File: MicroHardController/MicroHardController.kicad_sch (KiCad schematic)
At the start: 4 parts, among them J1 Conn_01x07_Pin, SW1 SW_Push_LED, U1 THB001P

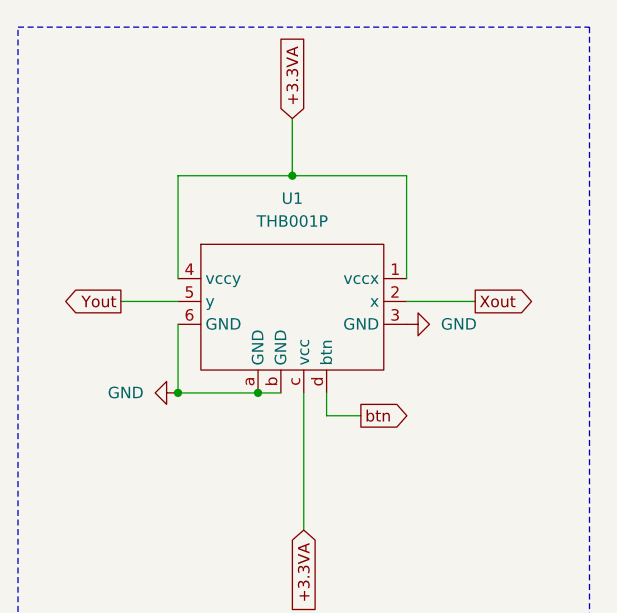
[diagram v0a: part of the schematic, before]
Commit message: feat: microhard controller schematic
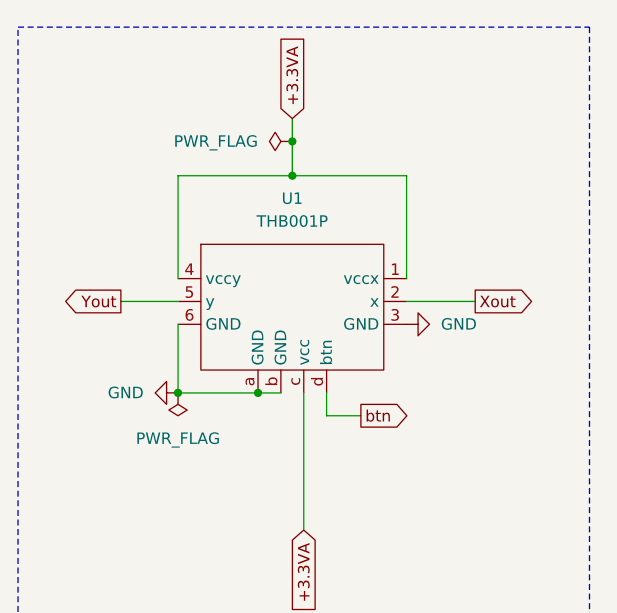
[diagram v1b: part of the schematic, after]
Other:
- company: (none) -> MicroHard
- title: (none) -> MicroHard FlightSimulator Controller

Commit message: feat: controller pcb layout
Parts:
- removed RV1: R_Potentiometer, symbol Device:R_Potentiometer
- added VR1: PS100-1B1BR10K, MicroHard:TRIM_PS100-1B1BR10K, symbol PS100-1B1BR10K:PS100-1B1BR10K
- J1: footprint (none) -> Connector_PinHeader_2.54mm:PinHeader_1x07_P2.54mm_Vertical
- SW1: footprint (none) -> Connector_PinHeader_2.54mm:PinHeader_1x04_P2.54mm_Vertical
- U1: footprint (none) -> MicroHard:CNK_THB001P
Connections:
- net +3.3VA: now also U1.VR1_1 (vccx), U1.VR2_1 (vccy), VR1.1; no longer U1.1 (vccx), U1.4 (vccy), U1.c (vcc)
- net GND: now also U1.VR1_3 (GND), U1.VR2_3 (GND), VR1.3; no longer U1.3 (GND), U1.6 (GND), U1.a (GND), U1.b (GND)
- net Xout: now also U1.VR1_2 (x); no longer U1.2 (x)
- net Yout: now also U1.VR2_2 (y); no longer U1.5 (y)
- net Zout: now also VR1.2
- net btn: no longer names the net of J1.7 (Pin_7)
- net btn: no longer U1.d (btn)
- no-connect marks 0 -> 5

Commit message: fix: controller fix
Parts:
- added R1, R2: 100K, symbol Device:R
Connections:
- net +3.3VA: now also U1.A (a)
- net GND: now also R1.2, R2.2
- net Button2: now reaches J1.7 (Pin_7)
- net Button2: now also U1.D (d), R1.1
- net Fbtn renamed Button1
- net Button1: now also R2.1
- no-connect marks 5 -> 2
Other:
- moved on the sheet: SW1

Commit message: feat: controller fixed
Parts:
- R1, R2: footprint (none) -> Resistor_SMD:R_1206_3216Metric_Pad1.30x1.75mm_HandSolder
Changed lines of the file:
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@@
 			)
 		)
-		(property "Footprint" ""
+		(property "Footprint" "Resistor_SMD:R_1206_3216Metric_Pad1.30x1.75mm_HandSolder"
 			(at 169.672 96.52 90)
 			(effects
@@
 			)
 		)
-		(property "Footprint" ""
+		(property "Footprint" "Resistor_SMD:R_1206_3216Metric_Pad1.30x1.75mm_HandSolder"
 			(at 68.58 108.458 90)
 			(effects
